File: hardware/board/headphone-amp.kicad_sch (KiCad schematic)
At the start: 15 parts, among them J6 Headphones, U1 MAX97220C, U2 74LVC1G04

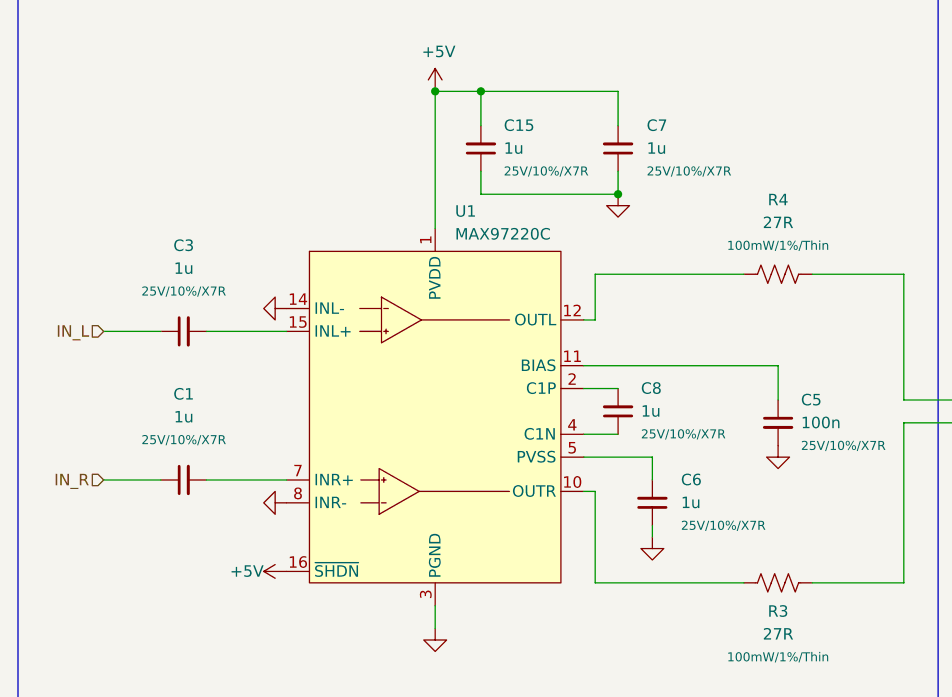
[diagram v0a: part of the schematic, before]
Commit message: Hardware v10:
- Replaced EOL 5V DC-DC converter with new TI part.
- Re-drawn schematic to current Winterbloom standards and style.
- Improved layout and color-coding.
- Updated branding and silk screen.
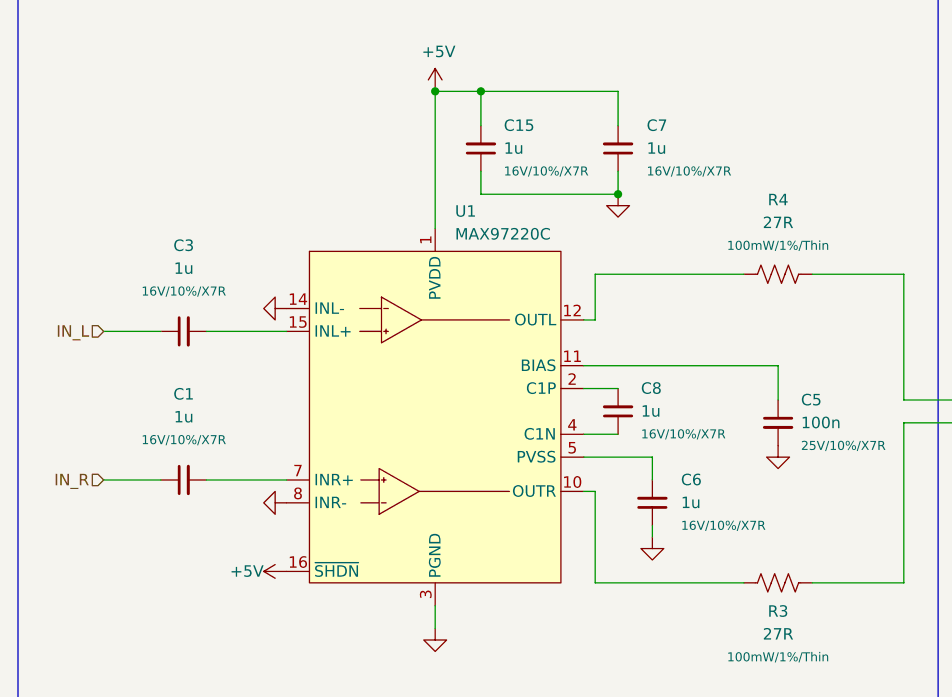
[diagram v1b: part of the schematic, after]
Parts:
- C1, C15, C3, C6, C7, C8: LCSC (none) -> C59782; MPN (none) -> CL10B105KO8NNNC; Notes Bulk cap -> Audio path; Rating 25V/10%/X7R -> 16V/10%/X7R
- C16, C5: LCSC (none) -> C1591; MPN (none) -> CL10B104KB8NNNC; Notes Bulk cap -> Bypass cap
- J6: Notes (none) -> Connects to external breakout. Jack: SJ-63083D; notes Connects to external breakout. Jack: SJ-63083D -> (none)
- R14, R15: LCSC 375503 -> C728638; MPN (none) -> RT0603FRE07100KL
- R3, R4: DigiKey YAG2323TR-ND -> (none); LCSC C375503 -> C863706; MPN RT0603FRE071KL -> RT0603FRE0727RL
- U1, U2: Substitutes Allowed (none) -> No
